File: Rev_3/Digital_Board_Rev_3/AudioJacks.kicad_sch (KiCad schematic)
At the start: 17 parts, among them J5 AudioJack3_Switch, J6 AudioJack3_Switch, J7 AudioJack3_Switch, J8 AudioJack3_Switch, K1 IM05, Q25 MMBT3904, SW4 SW_DIP_x02, U26A TLP222A-2, U26B TLP222A-2

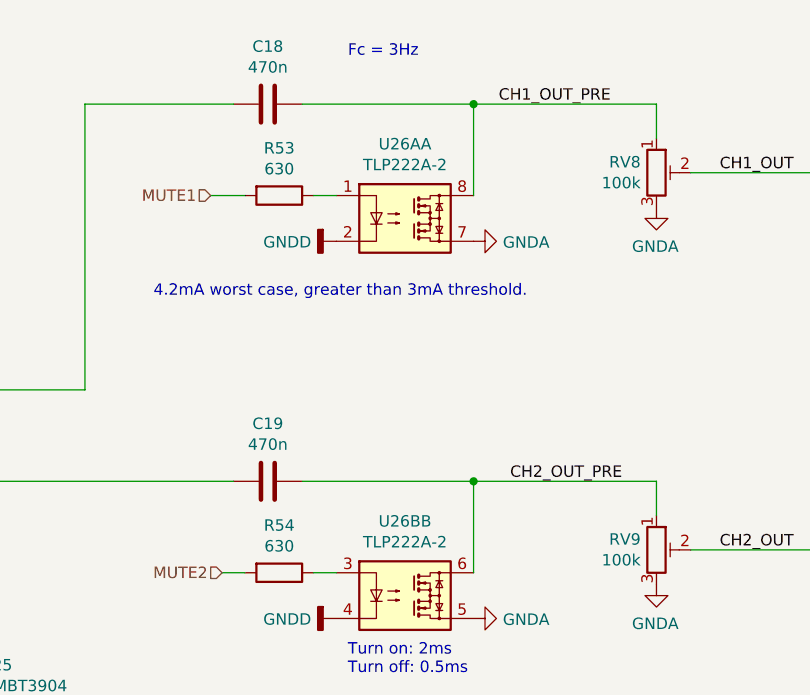
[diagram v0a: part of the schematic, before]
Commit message: Pivoting to Passive Jack Boards
Finalized layout for input/output Jack Boards, which are now completely passive and connected with board-to-board connectors. Schematics are not updated yet, just figuring out placement/dimensions.
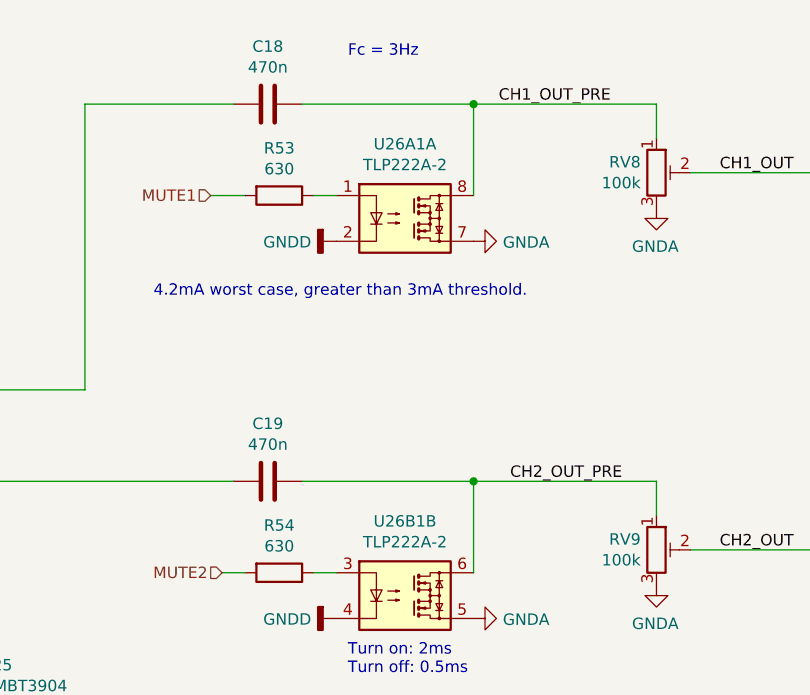
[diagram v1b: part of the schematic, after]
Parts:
- renumbered U26A to U26A1, U26B to U26B1
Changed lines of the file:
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@@
 		(on_board yes)
 		(dnp no)
-		(property "Reference" "U26A"
+		(property "Reference" "U26A1"
 			(at 157.48 33.655 0)
 			(effects
@@
 			(project "Digital Board Rev 2"
 				(path "/961bce4d-0f15-4753-8332-e4f92c717c57/00000000-0000-0000-0000-00006049dce2"
-					(reference "U26A")
+					(reference "U26A1")
 					(unit 1)
 				)
@@
 		(on_board yes)
 		(dnp no)
-		(property "Reference" "U26B"
+		(property "Reference" "U26B1"
 			(at 157.48 75.565 0)
 			(effects
@@
 			(project "Digital Board Rev 2"
 				(path "/961bce4d-0f15-4753-8332-e4f92c717c57/00000000-0000-0000-0000-00006049dce2"
-					(reference "U26B")
+					(reference "U26B1")
 					(unit 2)
 				)
